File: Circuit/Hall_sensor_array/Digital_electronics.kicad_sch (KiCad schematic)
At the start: 1 part, among them U273 ESP32-WROVER-IE-N8R8

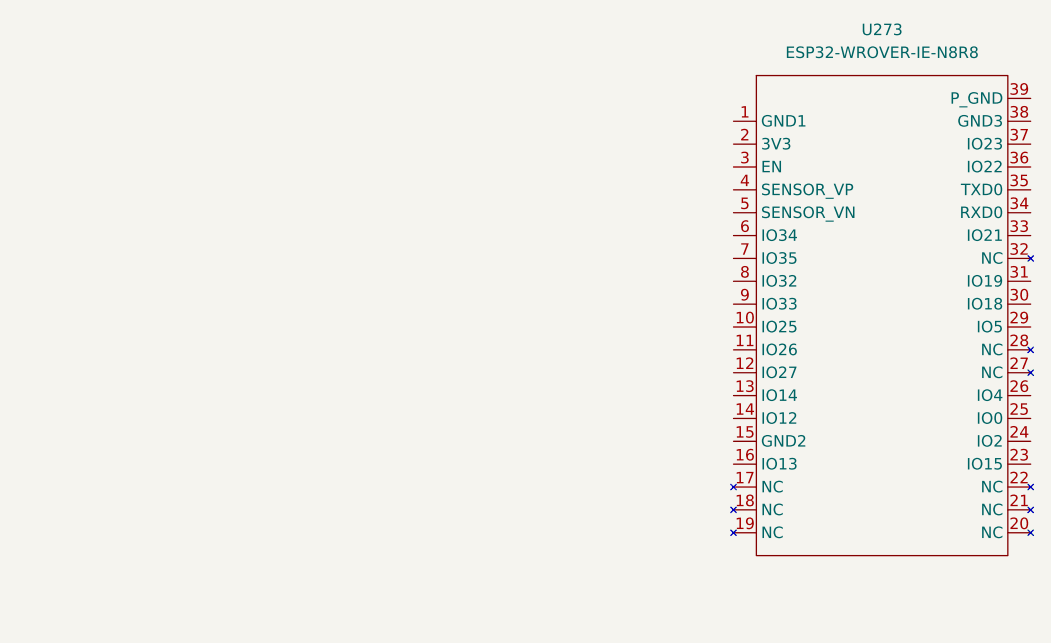
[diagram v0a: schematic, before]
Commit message: Updated circuit
Added binary counter for selecting analog multiplexer address
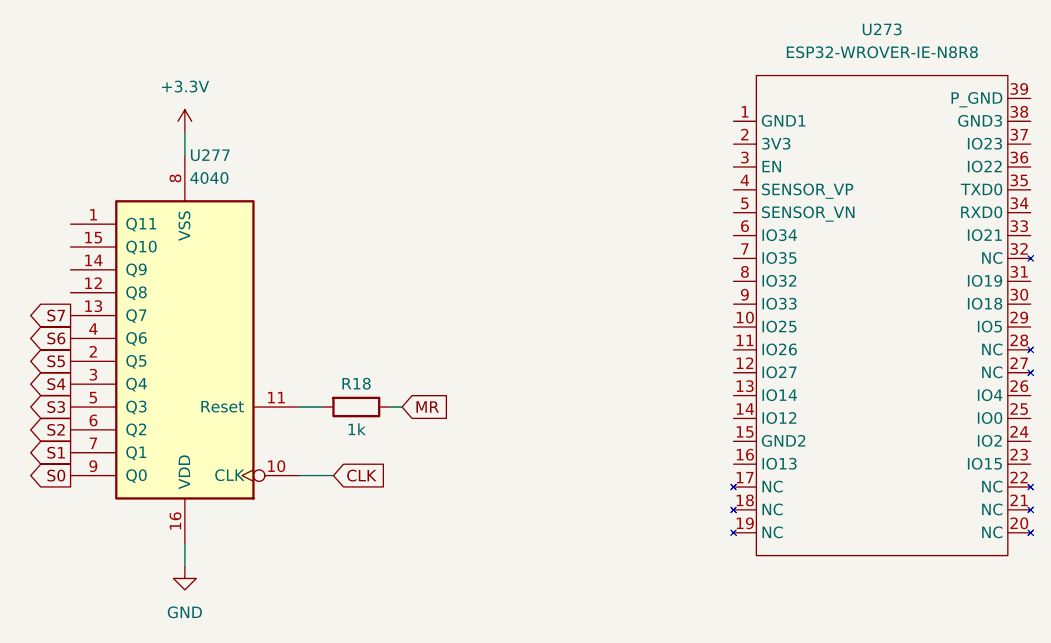
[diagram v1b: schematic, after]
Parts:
- added R18: 1k, symbol Device:R
- added U277: 4040, Package_SO:SOIC-16_3.9x9.9mm_P1.27mm, symbol 4xxx:4040
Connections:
- new net: R18.2, U277.11 (Reset)
- new net +3.3V: U277.8 (VSS)
- new net CLK: U277.10 (CLK)
- new net GND: U277.16 (VDD)
- new net MR: R18.1
- new net S0: U277.9 (Q0)
- new net S1: U277.7 (Q1)
- new net S2: U277.6 (Q2)
- new net S3: U277.5 (Q3)
- new net S4: U277.3 (Q4)
- new net S5: U277.2 (Q5)
- new net S6: U277.4 (Q6)
- new net S7: U277.13 (Q7)
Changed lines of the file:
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@@
 (kicad_sch (version 20211123) (generator eeschema)
   (paper "A4")
+  (wire (pts (xy 71.12 91.44) (xy 74.93 91.44))
+    (stroke (width 0) (type default) (color 0 0 0 0))
+  )
+  (wire (pts (xy 73.66 83.82) (xy 71.12 83.82))
+    (stroke (width 0) (type default) (color 0 0 0 0))
+  )
+  (wire (pts (xy 58.42 53.34) (xy 58.42 55.88))
+    (stroke (width 0) (type default) (color 0 0 0 0))
+  )
+  (wire (pts (xy 58.42 99.06) (xy 58.42 101.6))
+    (stroke (width 0) (type default) (color 0 0 0 0))
+  )
+  (wire (pts (xy 82.55 83.82) (xy 81.28 83.82))
+    (stroke (width 0) (type default) (color 0 0 0 0))
+  )
+  (global_label "S6" (shape output) (at 45.72 76.2 180) (fields_autoplaced)
+    (effects (font (size 1.27 1.27)) (justify right))
+    (property "Intersheet References" "${INTERSHEET_REFS}" (id 0) (at 40.8879 76.2794 0)
+      (effects (font (size 1.27 1.27)) (justify right) hide)
+    )
+  )
+  (global_label "S2" (shape output) (at 45.72 86.36 180) (fields_autoplaced)
+    (effects (font (size 1.27 1.27)) (justify right))
+    (property "Intersheet References" "${INTERSHEET_REFS}" (id 0) (at 40.8879 86.4394 0)
+      (effects (font (size 1.27 1.27)) (justify right) hide)
+    )
+  )
+  (global_label "MR" (shape input) (at 82.55 83.82 0) (fields_autoplaced)
+    (effects (font (size 1.27 1.27)) (justify left))
+    (property "Intersheet References" "${INTERSHEET_REFS}" (id 0) (at 87.6845 83.7406 0)
+      (effects (font (size 1.27 1.27)) (justify left) hide)
+    )
+  )
+  (global_label "S5" (shape output) (at 45.72 78.74 180) (fields_autoplaced)
+    (effects (font (size 1.27 1.27)) (justify right))
+    (property "Intersheet References" "${INTERSHEET_REFS}" (id 0) (at 40.8879 78.8194 0)
+      (effects (font (size 1.27 1.27)) (justify right) hide)
+    )
+  )
+  (global_label "S1" (shape output) (at 45.72 88.9 180) (fields_autoplaced)
+    (effects (font (size 1.27 1.27)) (justify right))
+    (property "Intersheet References" "${INTERSHEET_REFS}" (id 0) (at 40.8879 88.9794 0)
+      (effects (font (size 1.27 1.27)) (justify right) hide)
+    )
+  )
+  (global_label "S4" (shape output) (at 45.72 81.28 180) (fields_autoplaced)
+    (effects (font (size 1.27 1.27)) (justify right))
+    (property "Intersheet References" "${INTERSHEET_REFS}" (id 0) (at 40.8879 81.3594 0)
+      (effects (font (size 1.27 1.27)) (justify right) hide)
+    )
+  )
+  (global_label "S7" (shape output) (at 45.72 73.66 180) (fields_autoplaced)
+    (effects (font (size 1.27 1.27)) (justify right))
+    (property "Intersheet References" "${INTERSHEET_REFS}" (id 0) (at 40.8879 73.7394 0)
+      (effects (font (size 1.27 1.27)) (justify right) hide)
+    )
+  )
+  (global_label "S3" (shape output) (at 45.72 83.82 180) (fields_autoplaced)
+    (effects (font (size 1.27 1.27)) (justify right))
+    (property "Intersheet References" "${INTERSHEET_REFS}" (id 0) (at 40.8879 83.8994 0)
+      (effects (font (size 1.27 1.27)) (justify right) hide)
+    )
+  )
+  (global_label "S0" (shape output) (at 45.72 91.44 180) (fields_autoplaced)
+    (effects (font (size 1.27 1.27)) (justify right))
+    (property "Intersheet References" "${INTERSHEET_REFS}" (id 0) (at 40.8879 91.5194 0)
+      (effects (font (size 1.27 1.27)) (justify right) hide)
+    )
+  )
+  (global_label "CLK" (shape input) (at 74.93 91.44 0) (fields_autoplaced)
+    (effects (font (size 1.27 1.27)) (justify left))
+    (property "Intersheet References" "${INTERSHEET_REFS}" (id 0) (at 80.9112 91.3606 0)
+      (effects (font (size 1.27 1.27)) (justify left) hide)
+    )
+  )
   (symbol (lib_id "Custom_model:ESP32-WROVER-IE-N8R8") (at 135.89 59.69 0) (unit 1)
     (in_bom yes) (on_board yes)
@@
     (pin "9")
   )
+  (symbol (lib_id "4xxx:4040") (at 58.42 78.74 180) (unit 1)
+    (in_bom yes) (on_board yes) (fields_autoplaced)
+    (property "Reference" "U277" (id 0) (at 58.9406 55.88 0)
+      (effects (font (size 1.27 1.27)) (justify right))
+    )
+    (property "Value" "4040" (id 1) (at 58.9406 58.42 0)
+      (effects (font (size 1.27 1.27)) (justify right))
+    )
+    (property "Footprint" "Package_SO:SOIC-16_3.9x9.9mm_P1.27mm" (id 2) (at 58.42 78.74 0)
+      (effects (font (size 1.27 1.27)) hide)
+    )
+    (property "Datasheet" "http://www.intersil.com/content/dam/Intersil/documents/cd40/cd4020bms-24bms-40bms.pdf" (id 3) (at 58.42 78.74 0)
+      (effects (font (size 1.27 1.27)) hide)
+    )
+    (pin "1")
+    (pin "10")
+    (pin "11")
+    (pin "12")
+    (pin "13")
+    (pin "14")
+    (pin "15")
+    (pin "16")
+    (pin "2")
+    (pin "3")
+    (pin "4")
+    (pin "5")
+    (pin "6")
+    (pin "7")
+    (pin "8")
+    (pin "9")
+  )
+  (symbol (lib_id "power:GND") (at 58.42 101.6 0) (unit 1)
+    (in_bom yes) (on_board yes) (fields_autoplaced)
+    (property "Reference" "#PWR0650" (id 0) (at 58.42 107.95 0)
+      (effects (font (size 1.27 1.27)) hide)
+    )
+    (property "Value" "GND" (id 1) (at 58.42 106.68 0))
+    (property "Footprint" "" (id 2) (at 58.42 101.6 0)
+      (effects (font (size 1.27 1.27)) hide)
+    )
+    (property "Datasheet" "" (id 3) (at 58.42 101.6 0)
+      (effects (font (size 1.27 1.27)) hide)
+    )
+    (pin "1")
+  )
+  (symbol (lib_id "Device:R") (at 77.47 83.82 270) (unit 1)
+    (in_bom yes) (on_board yes)
+    (property "Reference" "R18" (id 0) (at 77.47 81.28 90))
+    (property "Value" "1k" (id 1) (at 77.47 86.36 90))
+    (property "Footprint" "" (id 2) (at 77.47 82.042 90)
+      (effects (font (size 1.27 1.27)) hide)
+    )
+    (property "Datasheet" "~" (id 3) (at 77.47 83.82 0)
+      (effects (font (size 1.27 1.27)) hide)
+    )
+    (pin "1")
+    (pin "2")
+  )
+  (symbol (lib_id "power:+3.3V") (at 58.42 53.34 0) (unit 1)
+    (in_bom yes) (on_board yes) (fields_autoplaced)
+    (property "Reference" "#PWR?" (id 0) (at 58.42 57.15 0)
+      (effects (font (size 1.27 1.27)) hide)
+    )
+    (property "Value" "+3.3V" (id 1) (at 58.42 48.26 0))
+    (property "Footprint" "" (id 2) (at 58.42 53.34 0)
+      (effects (font (size 1.27 1.27)) hide)
+    )
+    (property "Datasheet" "" (id 3) (at 58.42 53.34 0)
+      (effects (font (size 1.27 1.27)) hide)
+    )
+    (pin "1")
+  )
 )
